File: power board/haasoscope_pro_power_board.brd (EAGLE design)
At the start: 77.5 x 97.5 mm, 106 parts, among them IC1 TPS5430DDAR, IC10 TPS5430DDAR, IC11 TPS7A7200RGTR, IC12 TPS7A7200RGTR, IC14 TPS7A7200RGTR, IC2 TPS5430DDAR, IC3 TPS7A7200RGTR, IC4 TPS5430DDAR, IC5 TPS72325DBVR, IC6 TPS5430DDAR, IC7 TPS7A7200RGTR, IC8 TPS5430DDAR, IC9 TPS7A7200RGTR, J1 2p-2.54, J10 2p-2.54, J11 2p-2.54, J12 2p-2.54, J13 2p-2.54, J15 2p-2.54, J16 8pin, J2 2p-2.54, J3 2p-2.54, J4 2p-2.54, J5 2p-2.54, J6 2p-2.54, J7 2p-2.54, J8 2p-2.54, J9 2p-2.54

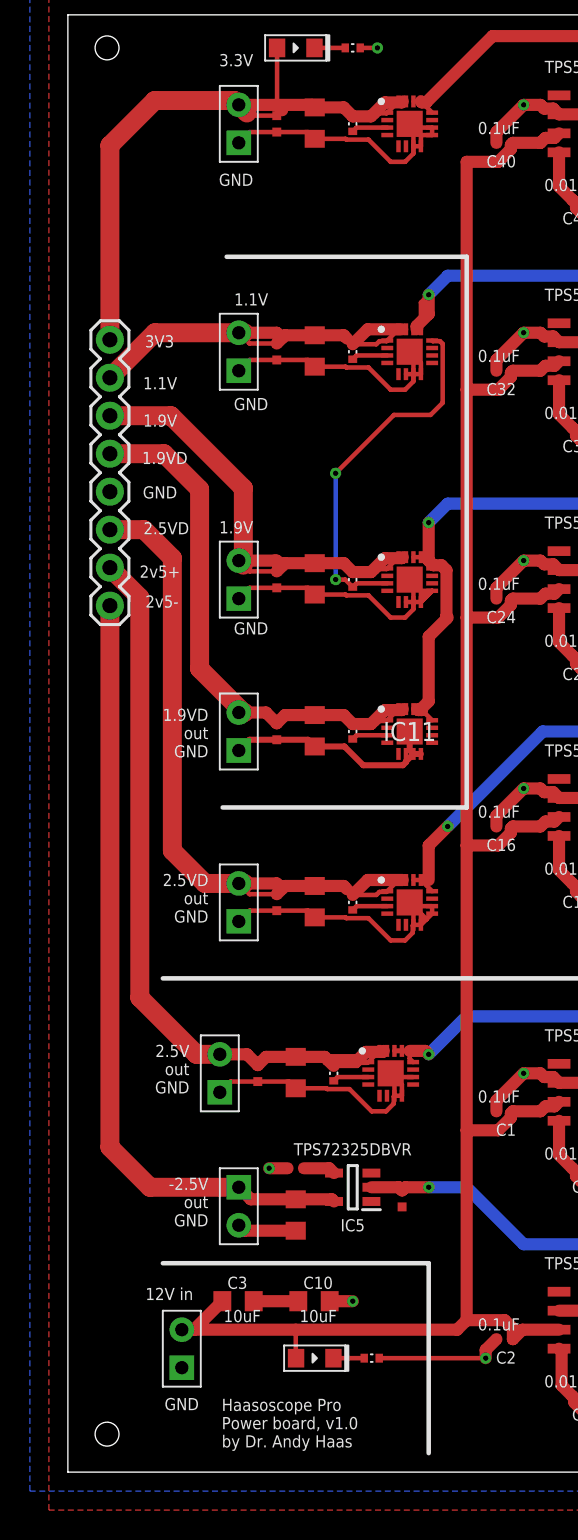
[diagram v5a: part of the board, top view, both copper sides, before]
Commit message: Power board v1.11 with +0.1V options, 2v5, etc.
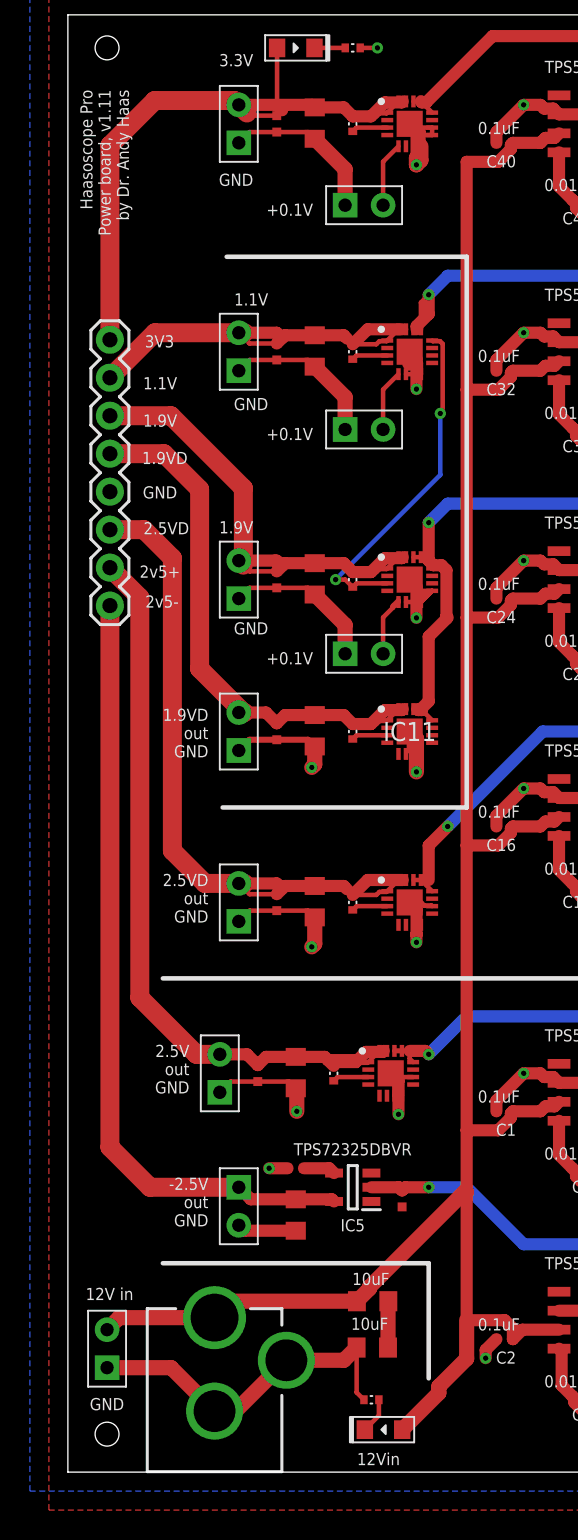
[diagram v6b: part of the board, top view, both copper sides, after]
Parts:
- added CN1: 12Vin, adafruit:DCJACK_2MM_PTH
- added J17, J18, J19: 2p-2.54, Seeed-Connector:H2-2.54
- moved C3 9.00 mm to (16.6, 12.7)
- moved D3 6.63 mm to (17.3, 4.11), turned to 0 degrees
- moved J3 5.00 mm to (-1.19, 9.53)
- moved C10 4.90 mm to (16.5, 9.60), turned to 180 degrees
- moved R14 2.78 mm to (16.5, 6.11), turned to 0 degrees
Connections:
- new net N$10: IC7.5, J17.2
- new net N$8: IC3.5, J19.2
- new net N$9: IC9.5, J18.2
- net GND: now also CN1.GND, CN1.GNDBREAK, J17.1, J18.1, J19.1; no longer IC14.9
- net VIN: now also CN1.PWR
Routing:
- net VIN: track 145.3 -> 157.6 mm
- net N$10: track 0.00 -> 4.67 mm
- net N$8: track 0.00 -> 4.37 mm
- net N$9: track 0.00 -> 4.13 mm
- net PG1V9: track 24.7 -> 23.4 mm
- net GND: track 241.4 -> 242.1 mm, vias 26 -> 34
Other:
- board text added: "+0.1V"
- board text added: "Haasoscope Pro Power board, v1.11 by Dr. Andy Haas"
- board text removed: "Haasoscope Pro Power board, v1.0 by Dr. Andy Haas"
